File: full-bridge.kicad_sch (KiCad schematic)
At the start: 13 parts, among them U801 VNH7070ASTR

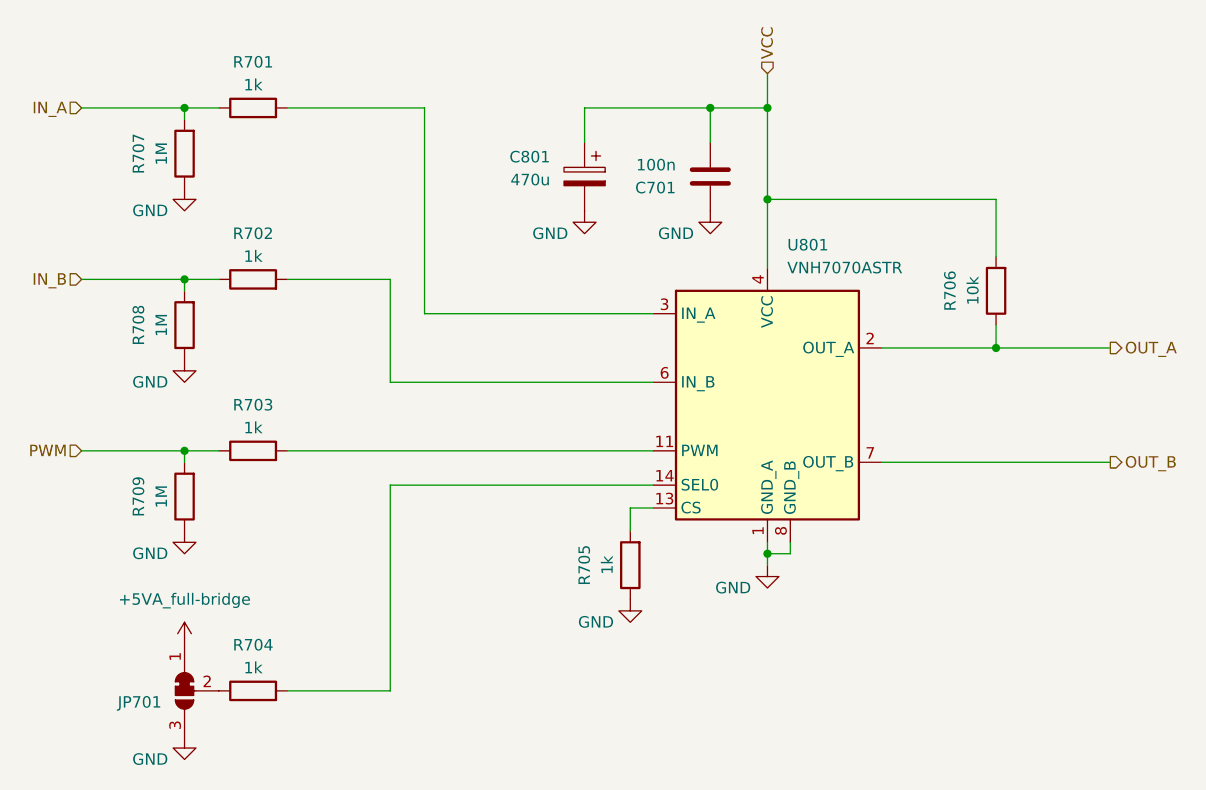
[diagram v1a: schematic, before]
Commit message: add enclosure output connectors
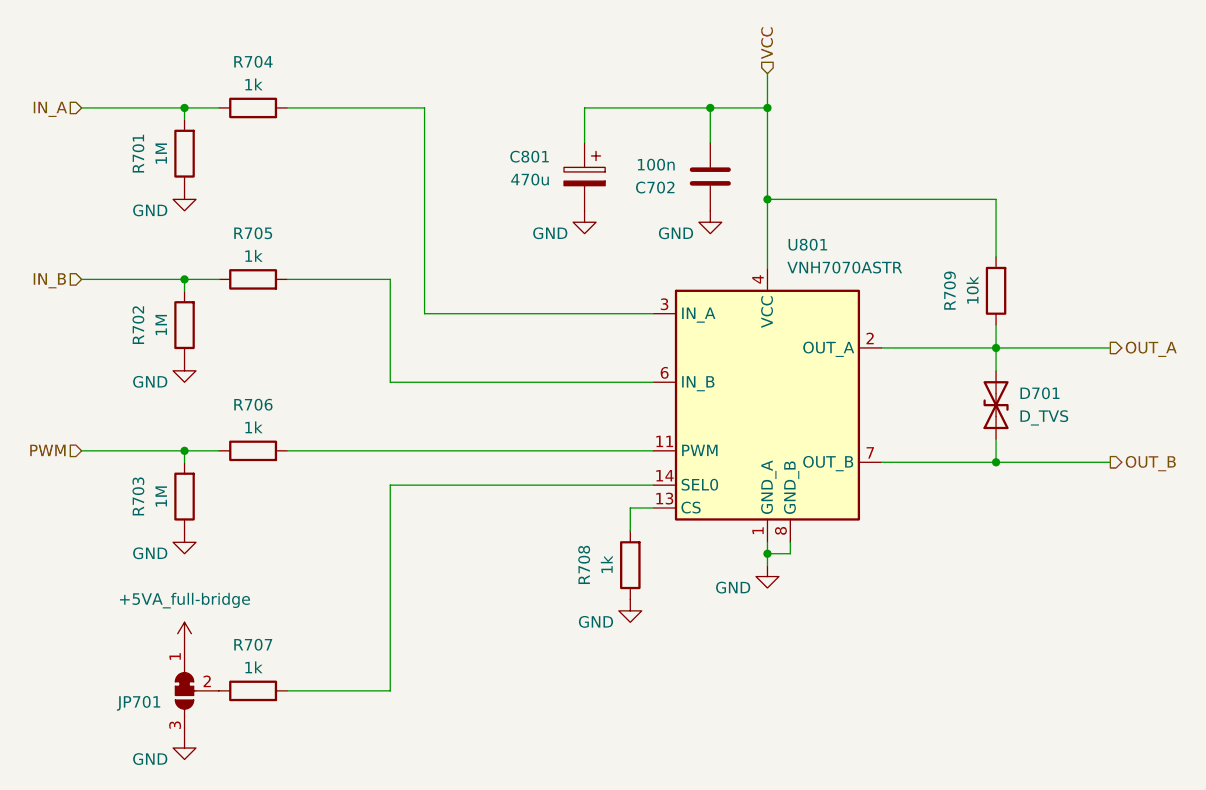
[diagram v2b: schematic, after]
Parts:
- added D701: D_TVS, pss:D_SOD-323_HandSoldering, symbol enclosure:D_TVS
- renumbered C701 to C702, R707 to R701, R708 to R702, R709 to R703, R701 to R704, R702 to R705, R703 to R706, R704 to R707, R705 to R708, R706 to R709
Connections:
- net OUT_A: now also D701.2 (A2)
- net OUT_B: now also D701.1 (A1)
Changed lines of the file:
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@@
 	(title_block
 		(title "Power Supply Sink")
-		(date "2025-02-20")
-		(rev "0.5.0")
+		(date "2025-02-21")
+		(rev "1.0.0")
 		(company "Open Battery Tester")
 		(comment 1 "Full Bridge")
@@
 		(color 0 0 0 0)
 	)
+	(junction
+		(at 177.8 114.3)
+		(diameter 0)
+		(color 0 0 0 0)
+	)
 	(wire
 		(pts
@@
 	(wire
 		(pts
-			(xy 165.1 114.3) (xy 190.5 114.3)
+			(xy 177.8 101.6) (xy 177.8 104.14)
+		)
+		(stroke
+			(width 0)
+			(type default)
+		)
+	)
+	(wire
+		(pts
+			(xy 165.1 114.3) (xy 177.8 114.3)
 		)
 		(stroke
@@
 	(wire
 		(pts
+			(xy 177.8 111.76) (xy 177.8 114.3)
+		)
+		(stroke
+			(width 0)
+			(type default)
+		)
+	)
+	(wire
+		(pts
 			(xy 177.8 91.44) (xy 177.8 85.09)
 		)
@@
 		(pts
 			(xy 87.63 93.98) (xy 91.44 93.98)
+		)
+		(stroke
+			(width 0)
+			(type default)
+		)
+	)
+	(wire
+		(pts
+			(xy 177.8 114.3) (xy 190.5 114.3)
 		)
 		(stroke
@@
 		(on_board yes)
 		(dnp no)
-		(property "Reference" "#PWR0702"
+		(property "Reference" "#PWR0707"
 			(at 137.16 135.89 0)
 			(effects
@@
 			(project "enclosure"
 				(path "/8ec0899b-9d7b-491d-933a-49b74b34a0df/bbda67e3-2151-48ab-90c3-bcc692138389"
-					(reference "#PWR0702")
+					(reference "#PWR0707")
 					(unit 1)
 				)
@@
 		(on_board yes)
 		(dnp no)
-		(property "Reference" "#PWR0705"
+		(property "Reference" "#PWR0701"
 			(at 87.63 90.17 0)
 			(effects
@@
 			(project "enclosure"
 				(path "/8ec0899b-9d7b-491d-933a-49b74b34a0df/bbda67e3-2151-48ab-90c3-bcc692138389"
-					(reference "#PWR0705")
+					(reference "#PWR0701")
 					(unit 1)
 				)
@@
 		(on_board yes)
 		(dnp no)
-		(property "Reference" "R709"
+		(property "Reference" "R703"
 			(at 82.55 118.11 90)
 			(effects
@@
 			(project "enclosure"
 				(path "/8ec0899b-9d7b-491d-933a-49b74b34a0df/bbda67e3-2151-48ab-90c3-bcc692138389"
-					(reference "R709")
+					(reference "R703")
 					(unit 1)
 				)
@@
 		(on_board yes)
 		(dnp no)
-		(property "Reference" "#PWR0704"
+		(property "Reference" "#PWR0702"
 			(at 87.63 109.22 0)
 			(effects
@@
 			(project "enclosure"
 				(path "/8ec0899b-9d7b-491d-933a-49b74b34a0df/bbda67e3-2151-48ab-90c3-bcc692138389"
-					(reference "#PWR0704")
+					(reference "#PWR0702")
 					(unit 1)
 				)
@@
 		(on_board yes)
 		(dnp no)
-		(property "Reference" "C701"
+		(property "Reference" "C702"
 			(at 142.24 83.8201 0)
 			(effects
@@
 			(project "enclosure"
 				(path "/8ec0899b-9d7b-491d-933a-49b74b34a0df/bbda67e3-2151-48ab-90c3-bcc692138389"
-					(reference "C701")
+					(reference "C702")
 					(unit 1)
 				)
@@
 		(on_board yes)
 		(dnp no)
-		(property "Reference" "R708"
+		(property "Reference" "R702"
 			(at 82.55 99.06 90)
 			(effects
@@
 			(project "enclosure"
 				(path "/8ec0899b-9d7b-491d-933a-49b74b34a0df/bbda67e3-2151-48ab-90c3-bcc692138389"
-					(reference "R708")
+					(reference "R702")
 					(unit 1)
 				)
@@
 					(unit 1)
 				)
+				(path "/8ec0899b-9d7b-491d-933a-49b74b34a0df/bbda67e3-2151-48ab-90c3-bcc692138389"
+					(reference "C701")
+					(unit 1)
+				)
 			)
 		)
@@
 		(on_board yes)
 		(dnp no)
-		(property "Reference" "R703"
+		(property "Reference" "R706"
 			(at 95.25 107.95 90)
 			(effects
@@
 			(project "enclosure"
 				(path "/8ec0899b-9d7b-491d-933a-49b74b34a0df/bbda67e3-2151-48ab-90c3-bcc692138389"
-					(reference "R703")
+					(reference "R706")
 					(unit 1)
 				)
@@
 					(unit 1)
 				)
+				(path "/8ec0899b-9d7b-491d-933a-49b74b34a0df/bbda67e3-2151-48ab-90c3-bcc692138389"
+					(reference "#PWR0704")
+					(unit 1)
+				)
 			)
 		)
@@
 		(on_board yes)
 		(dnp no)
-		(property "Reference" "#PWR0706"
+		(property "Reference" "#PWR0705"
 			(at 87.63 151.13 0)
 			(effects
@@
 			(project "enclosure"
 				(path "/8ec0899b-9d7b-491d-933a-49b74b34a0df/bbda67e3-2151-48ab-90c3-bcc692138389"
-					(reference "#PWR0706")
+					(reference "#PWR0705")
 					(unit 1)
 				)
@@
 				(path "/8ec0899b-9d7b-491d-933a-49b74b34a0df/778c7cc2-ff27-4288-861b-5b98ae270a8f"
 					(reference "#PWR0905")
+					(unit 1)
+				)
+			)
+		)
+	)
+	(symbol
+		(lib_id "enclosure:D_TVS")
+		(at 177.8 107.95 90)
+		(unit 1)
+		(exclude_from_sim no)
+		(in_bom yes)
+		(on_board yes)
+		(dnp no)
+		(fields_autoplaced yes)
+		(property "Reference" "D701"
+			(at 180.34 106.6799 90)
+			(effects
+				(font
+					(size 1.27 1.27)
+				)
+				(justify right)
+			)
+		)
+		(property "Value" "D_TVS"
+			(at 180.34 109.2199 90)
+			(effects
+				(font
+					(size 1.27 1.27)
+				)
+				(justify right)
+			)
+		)
+		(property "Footprint" "pss:D_SOD-323_HandSoldering"
+			(at 177.8 107.95 0)
+			(effects
+				(font
+					(size 1.27 1.27)
+				)
+				(hide yes)
+			)
+		)
+		(property "Datasheet" "./datasheet/UDD32C15L01.pdf"
+			(at 177.8 107.95 0)
+			(effects
+				(font
+					(size 1.27 1.27)
+				)
+				(hide yes)
+			)
+		)
+		(property "Description" "Bidirectional transient-voltage-suppression diode"
+			(at 177.8 107.95 0)
+			(effects
+				(font
+					(size 1.27 1.27)
+				)
+				(hide yes)
+			)
+		)
+		(property "MPN" "UDD32C24L01"
+			(at 177.8 107.95 0)
+			(effects
+				(font
+					(size 1.27 1.27)
+				)
+				(hide yes)
+			)
+		)
+		(property "VPN" "603-UDD32C24L01"
+			(at 177.8 107.95 0)
+			(effects
+				(font
+					(size 1.27 1.27)
+				)
+				(hide yes)
+			)
+		)
+		(pin "1"
+		)
+		(pin "2"
+		)
+		(instances
+			(project "enclosure"
+				(path "/8ec0899b-9d7b-491d-933a-49b74b34a0df/bbda67e3-2151-48ab-90c3-bcc692138389"
+					(reference "D701")
+					(unit 1)
+				)
+				(path "/8ec0899b-9d7b-491d-933a-49b74b34a0df/0b6c8db3-fe41-474c-8239-e75ecc104b72"
+					(reference "D801")
+					(unit 1)
+				)
+				(path "/8ec0899b-9d7b-491d-933a-49b74b34a0df/778c7cc2-ff27-4288-861b-5b98ae270a8f"
+					(reference "D901")
 					(unit 1)
 				)
@@
 					(unit 1)
 				)
+				(path "/8ec0899b-9d7b-491d-933a-49b74b34a0df/bbda67e3-2151-48ab-90c3-bcc692138389"
+					(reference "U701")
+					(unit 1)
+				)
 			)
 		)
@@
 		(on_board yes)
 		(dnp no)
-		(property "Reference" "R707"
+		(property "Reference" "R701"
 			(at 82.55 80.01 90)
 			(effects
@@
 			(project "enclosure"
 				(path "/8ec0899b-9d7b-491d-933a-49b74b34a0df/bbda67e3-2151-48ab-90c3-bcc692138389"
-					(reference "R707")
+					(reference "R701")
 					(unit 1)
 				)
@@
 		(on_board yes)
 		(dnp no)
-		(property "Reference" "R706"
+		(property "Reference" "R709"
 			(at 172.72 95.25 90)
 			(effects
@@
 			(project "enclosure"
 				(path "/8ec0899b-9d7b-491d-933a-49b74b34a0df/bbda67e3-2151-48ab-90c3-bcc692138389"
-					(reference "R706")
+					(reference "R709")
 					(unit 1)
 				)
@@
 		(on_board yes)
 		(dnp no)
-		(property "Reference" "R701"
+		(property "Reference" "R704"
 			(at 95.25 69.85 90)
 			(effects
@@
 			(project "enclosure"
 				(path "/8ec0899b-9d7b-491d-933a-49b74b34a0df/bbda67e3-2151-48ab-90c3-bcc692138389"
-					(reference "R701")
+					(reference "R704")
 					(unit 1)
 				)
@@
 		(on_board yes)
 		(dnp no)
-		(property "Reference" "R704"
+		(property "Reference" "R707"
 			(at 95.25 134.62 90)
 			(effects
@@
 			(project "enclosure"
 				(path "/8ec0899b-9d7b-491d-933a-49b74b34a0df/bbda67e3-2151-48ab-90c3-bcc692138389"
-					(reference "R704")
+					(reference "R707")
 					(unit 1)
 				)
@@
 		(on_board yes)
 		(dnp no)
-		(property "Reference" "R702"
+		(property "Reference" "R705"
 			(at 95.25 88.9 90)
 			(effects
@@
 			(project "enclosure"
 				(path "/8ec0899b-9d7b-491d-933a-49b74b34a0df/bbda67e3-2151-48ab-90c3-bcc692138389"
-					(reference "R702")
+					(reference "R705")
 					(unit 1)
 				)
@@
 		(on_board yes)
 		(dnp no)
-		(property "Reference" "#PWR0707"
+		(property "Reference" "#PWR0708"
 			(at 146.05 92.71 0)
 			(effects
@@
 			(project "enclosure"
 				(path "/8ec0899b-9d7b-491d-933a-49b74b34a0df/bbda67e3-2151-48ab-90c3-bcc692138389"
-					(reference "#PWR0707")
+					(reference "#PWR0708")
 					(unit 1)
 				)
@@
 		(on_board yes)
 		(dnp no)
-		(property "Reference" "R705"
+		(property "Reference" "R708"
 			(at 132.08 125.73 90)
 			(effects
@@
 			(project "enclosure"
 				(path "/8ec0899b-9d7b-491d-933a-49b74b34a0df/bbda67e3-2151-48ab-90c3-bcc692138389"
-					(reference "R705")
+					(reference "R708")
 					(unit 1)
 				)
@@
 		(on_board yes)
 		(dnp no)
-		(property "Reference" "#PWR0709"
+		(property "Reference" "#PWR0706"
 			(at 132.08 92.71 0)
 			(effects
@@
 			(project "enclosure"
 				(path "/8ec0899b-9d7b-491d-933a-49b74b34a0df/bbda67e3-2151-48ab-90c3-bcc692138389"
-					(reference "#PWR0709")
+					(reference "#PWR0706")
 					(unit 1)
 				)
@@
 		(on_board yes)
 		(dnp no)
-		(property "Reference" "#PWR0701"
+		(property "Reference" "#PWR0709"
 			(at 152.4 132.08 0)
 			(effects
@@
 			(project "enclosure"
 				(path "/8ec0899b-9d7b-491d-933a-49b74b34a0df/bbda67e3-2151-48ab-90c3-bcc692138389"
-					(reference "#PWR0701")
-					(unit 1)
-				)
+					(reference "#PWR0709")
+					(unit 1)
+				)

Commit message: update datasheets and footprint references
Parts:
- C702: footprint pss:C_0805_2012Metric_Pad1.18x1.45mm_HandSolder -> enclosure:C_0805_2012Metric_Pad1.18x1.45mm_HandSolder
- C801: footprint Capacitor_SMD:CP_Elec_10x10 -> enclosure:CP_Elec_10x10
- D701: footprint pss:D_SOD-323_HandSoldering -> enclosure:D_SOD-323_HandSoldering
- JP701: footprint pss:SolderJumper-3_P1.3mm_Bridged12-Soldermask-Paste_RoundedPad1.0x1.5mm -> enclosure:SolderJumper-3_P1.3mm_Bridged12-Soldermask-Paste_RoundedPad1.0x1.5mm
- R701, R702, R703, R704, R705, R706, R707, R708, R709: footprint pss:R_1210_3225Metric_Pad1.30x2.65mm_HandSolder -> enclosure:R_1210_3225Metric_Pad1.30x2.65mm_HandSolder
- U801: footprint Package_SO:SO-16_3.9x9.9mm_P1.27mm -> enclosure:SO-16_3.9x9.9mm_P1.27mm
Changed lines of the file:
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@@
 			)
 		)
-		(property "Footprint" "pss:R_1210_3225Metric_Pad1.30x2.65mm_HandSolder"
+		(property "Footprint" "enclosure:R_1210_3225Metric_Pad1.30x2.65mm_HandSolder"
 			(at 89.408 118.11 90)
 			(effects
@@
 			)
 		)
-		(property "Footprint" "pss:C_0805_2012Metric_Pad1.18x1.45mm_HandSolder"
+		(property "Footprint" "enclosure:C_0805_2012Metric_Pad1.18x1.45mm_HandSolder"
 			(at 145.0848 78.74 0)
 			(effects
@@
 			)
 		)
-		(property "Footprint" "pss:R_1210_3225Metric_Pad1.30x2.65mm_HandSolder"
+		(property "Footprint" "enclosure:R_1210_3225Metric_Pad1.30x2.65mm_HandSolder"
 			(at 89.408 99.06 90)
 			(effects
@@
 			)
 		)
-		(property "Footprint" "Capacitor_SMD:CP_Elec_10x10"
+		(property "Footprint" "enclosure:CP_Elec_10x10"
 			(at 131.1148 86.36 0)
 			(effects
@@
 			)
 		)
-		(property "Footprint" "pss:R_1210_3225Metric_Pad1.30x2.65mm_HandSolder"
+		(property "Footprint" "enclosure:R_1210_3225Metric_Pad1.30x2.65mm_HandSolder"
 			(at 95.25 114.808 90)
 			(effects
@@
 			)
 		)
-		(property "Footprint" "pss:SolderJumper-3_P1.3mm_Bridged12-Soldermask-Paste_RoundedPad1.0x1.5mm"
+		(property "Footprint" "enclosure:SolderJumper-3_P1.3mm_Bridged12-Soldermask-Paste_RoundedPad1.0x1.5mm"
 			(at 87.63 139.7 0)
 			(effects
@@
 			)
 		)
-		(property "Footprint" "pss:D_SOD-323_HandSoldering"
+		(property "Footprint" "enclosure:D_SOD-323_HandSoldering"
 			(at 177.8 107.95 0)
 			(effects
@@
 			)
 		)
-		(property "Footprint" "Package_SO:SO-16_3.9x9.9mm_P1.27mm"
+		(property "Footprint" "enclosure:SO-16_3.9x9.9mm_P1.27mm"
 			(at 152.4 142.24 0)
 			(effects
@@
 			)
 		)
-		(property "Footprint" "pss:R_1210_3225Metric_Pad1.30x2.65mm_HandSolder"
+		(property "Footprint" "enclosure:R_1210_3225Metric_Pad1.30x2.65mm_HandSolder"
 			(at 89.408 80.01 90)
 			(effects
@@
 			)
 		)
-		(property "Footprint" "pss:R_1210_3225Metric_Pad1.30x2.65mm_HandSolder"
+		(property "Footprint" "enclosure:R_1210_3225Metric_Pad1.30x2.65mm_HandSolder"
 			(at 179.578 95.25 90)
 			(effects
@@
 			)
 		)
-		(property "Footprint" "pss:R_1210_3225Metric_Pad1.30x2.65mm_HandSolder"
+		(property "Footprint" "enclosure:R_1210_3225Metric_Pad1.30x2.65mm_HandSolder"
 			(at 95.25 76.708 90)
 			(effects
@@
 			)
 		)
-		(property "Footprint" "pss:R_1210_3225Metric_Pad1.30x2.65mm_HandSolder"
+		(property "Footprint" "enclosure:R_1210_3225Metric_Pad1.30x2.65mm_HandSolder"
 			(at 95.25 141.478 90)
 			(effects
@@
 			)
 		)
-		(property "Footprint" "pss:R_1210_3225Metric_Pad1.30x2.65mm_HandSolder"
+		(property "Footprint" "enclosure:R_1210_3225Metric_Pad1.30x2.65mm_HandSolder"
 			(at 95.25 95.758 90)
 			(effects
@@
 			)
 		)
-		(property "Footprint" "pss:R_1210_3225Metric_Pad1.30x2.65mm_HandSolder"
+		(property "Footprint" "enclosure:R_1210_3225Metric_Pad1.30x2.65mm_HandSolder"
 			(at 138.938 125.73 90)
 			(effects
